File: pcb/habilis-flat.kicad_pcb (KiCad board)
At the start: 2 copper layers, 164 x 172.3 mm, 74 parts, among them SW1 MX, SW10 MX, SW11 MX, SW12 MX, SW13 MX, SW14 MX, SW15 MX, SW16 MX, SW17 MX, SW18 MX, SW19 MX, SW2 MX, SW20 MX, SW21 MX, SW22 MX, SW23 MX, SW24 MX, SW25 MX, SW26 MX, SW27 MX, SW28 MX, SW29 MX, SW3 MX, SW30 MX, SW31 MX, SW32 MX, SW33 MX, SW34 MX, SW35 MX, SW4 MX, SW5 MX, SW6 MX, SW7 MX, SW8 MX, SW9 MX, U1 ProMicro

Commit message: Simplify schematic, update diode footprint reference
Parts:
- renumbered TRRS_L to J1, TRRS_R to J2
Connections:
- net Net-(D1-K) renamed row1
- net Net-(D10-K) renamed row5
- net Net-(D12-K) renamed row2
- net Net-(D13-K) renamed row3
- net Net-(D14-K) renamed row4
- net Net-(U1-B4) renamed col2
- net Net-(U1-B5) renamed col1
- net Net-(U1-C6) renamed col5
- net Net-(U1-D4) renamed col6
- net Net-(U1-D7) renamed col4
- net Net-(U1-E6) renamed col3
- net Net-(U1-F6) renamed col7

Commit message: Update PCB
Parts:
- TRRS1: renamed from J1; value AudioJack4 -> Left TRRS cable
- TRRS2: renamed from J2; value AudioJack4 -> Right TRRS cable

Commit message: Realign thumb cluster keys
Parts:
- moved SW31 19.6 mm to (125.3, 93.6)
- moved SW32 19.6 mm to (139.5, 107.3)
- moved D31 16.1 mm to (125.5, 90.0)
- moved D32 16.1 mm to (136.8, 101.5)
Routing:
- net row1: track 238.2 -> 220.3 mm
- net row2: track 221.3 -> 238.9 mm
- net Net-(D32-A): track 9.79 -> 7.63 mm
- net Net-(D31-A): track 7.63 -> 9.79 mm

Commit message: Cleanup some tracks
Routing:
- net row2: track 238.9 -> 245.7 mm

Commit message: Move copyright to a nicer place
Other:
- board text added: "(yet another"
- board text added: "keyboard)"
- board text added: "© Thibault Polge 2023 https://thb.lt"
- board text removed: "Copyright © 2023 Thibault Polge https://thb.lt/"
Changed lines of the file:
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@@
   (gr_line (start 149.588485 105.669449) (end 133.956727 96.644449)
     (stroke (width 0.2) (type solid)) (layer "Edge.Cuts"))
-  (gr_text "Copyright © 2023 Thibault Polge https://thb.lt/" (at 65.90965 48.470207 90) (layer "B.SilkS")
-    (effects (font (size 1 1) (thickness 0.15)) (justify left bottom mirror))
-  )
   (gr_text "FLAT" (at 54.541406 -12.165028) (layer "B.SilkS")
     (effects (font (size 2 2) (thickness 0.2)) (justify left bottom mirror))
@@
     (effects (font (size 2 2) (thickness 0.2)) (justify left bottom mirror))
   )
+  (gr_text "© Thibault Polge \n2023 https://thb.lt" (at 75.63002 -13.373041) (layer "B.SilkS")
+    (effects (font (size 1 1) (thickness 0.15)) (justify right bottom mirror))
+  )
+  (gr_text "(yet another\n" (at 82.886942 -19.195307) (layer "F.SilkS")
+    (effects (font (size 1 1) (thickness 0.15)) (justify bottom))
+  )
+  (gr_text "HABILIS" (at 81.410346 -20.657928) (layer "F.SilkS" knockout)
+    (effects (font (size 1 1) (thickness 0.15)) (justify left bottom))
+  )
+  (gr_text "keyboard)" (at 80.949201 -18.096012) (layer "F.SilkS")
+    (effects (font (size 1 1) (thickness 0.15)) (justify left bottom))
+  )
   (segment (start 1.27 2.54) (end 1.27 0.633604) (width 0.25) (layer "F.Cu") (net 1))

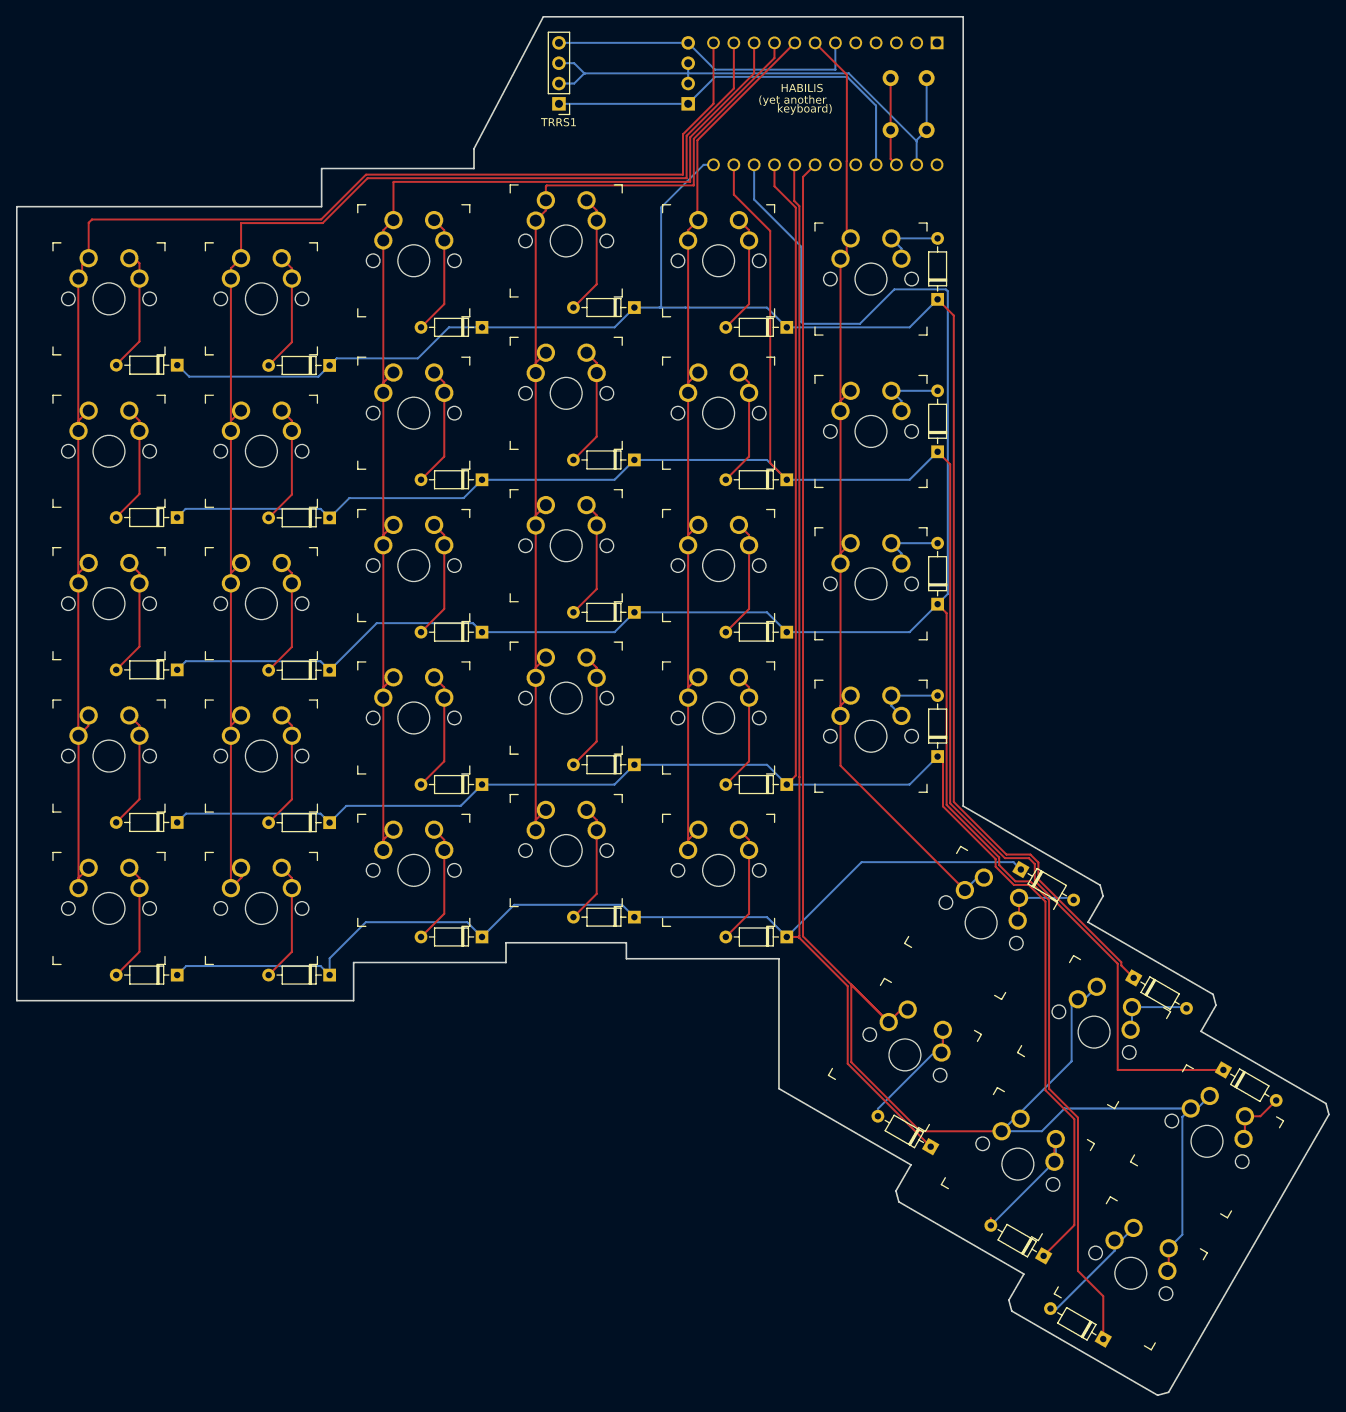
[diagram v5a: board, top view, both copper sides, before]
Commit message: Restore mounting holes
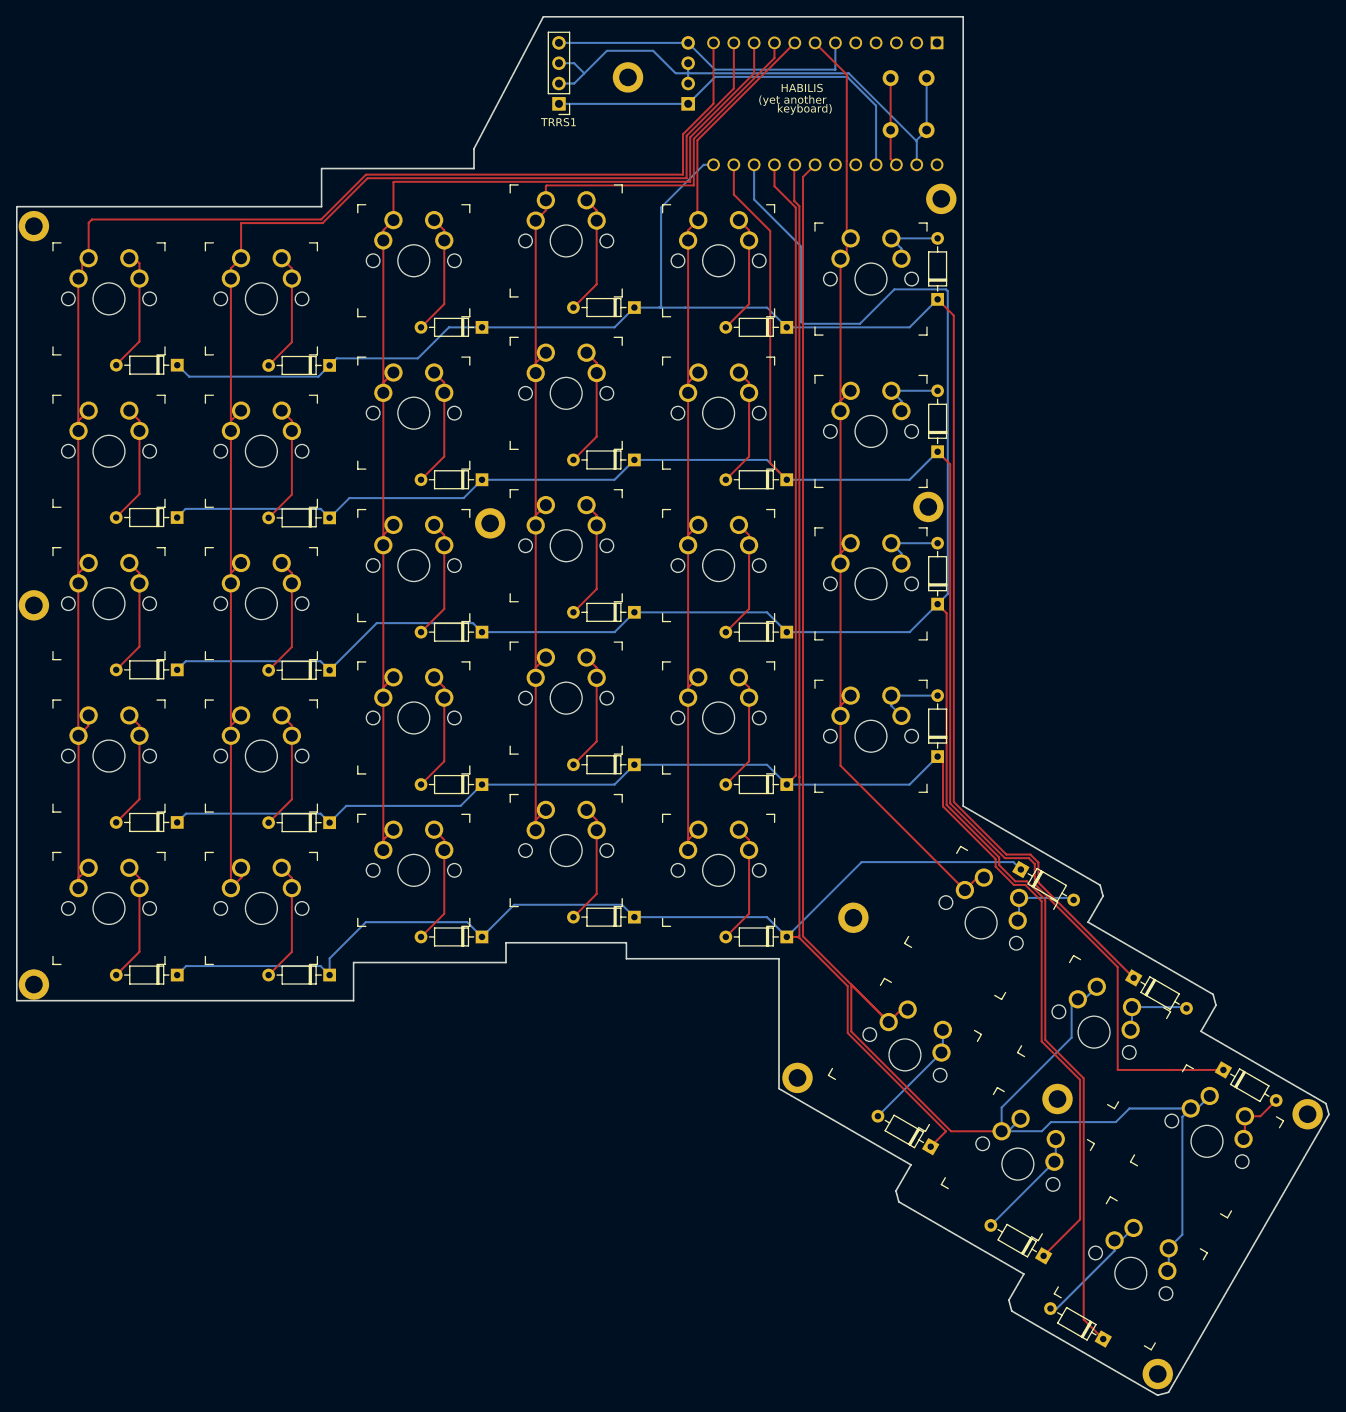
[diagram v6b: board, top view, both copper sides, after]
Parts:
- added REF**: MountingHole_2.2mm_M2_DIN965_Pad_NO_Silkscreem, project-components:MountingHole_2.2mm_M2_DIN965_Pad_NO_Silkscreem, F.Cu at (101.5, -7.41)
- added REF**: MountingHole_2.2mm_M2_DIN965_Pad_NO_Silkscreem, project-components:MountingHole_2.2mm_M2_DIN965_Pad_NO_Silkscreem, F.Cu at (83.5, 102.5)
- added REF**: MountingHole_2.2mm_M2_DIN965_Pad_NO_Silkscreem, project-components:MountingHole_2.2mm_M2_DIN965_Pad_NO_Silkscreem, F.Cu at (62.3, -22.6)
- added REF**: MountingHole_2.2mm_M2_DIN965_Pad_NO_Silkscreem, project-components:MountingHole_2.2mm_M2_DIN965_Pad_NO_Silkscreem, F.Cu at (128.6, 139.5)
- added REF**: MountingHole_2.2mm_M2_DIN965_Pad_NO_Silkscreem, project-components:MountingHole_2.2mm_M2_DIN965_Pad_NO_Silkscreem, F.Cu at (90.5, 82.4)
- added REF**: MountingHole_2.2mm_M2_DIN965_Pad_NO_Silkscreem, project-components:MountingHole_2.2mm_M2_DIN965_Pad_NO_Silkscreem, F.Cu at (99.9, 31.1)
- added REF**: MountingHole_2.2mm_M2_DIN965_Pad_NO_Silkscreem, project-components:MountingHole_2.2mm_M2_DIN965_Pad_NO_Silkscreem, F.Cu at (116.0, 105.1)
- added REF**: MountingHole_2.2mm_M2_DIN965_Pad_NO_Silkscreem, project-components:MountingHole_2.2mm_M2_DIN965_Pad_NO_Silkscreem, F.Cu at (147.3, 107.0)
- added REF**: MountingHole_2.2mm_M2_DIN965_Pad_NO_Silkscreem, project-components:MountingHole_2.2mm_M2_DIN965_Pad_NO_Silkscreem, F.Cu at (-11.9, 43.4)
- added REF**: MountingHole_2.2mm_M2_DIN965_Pad_NO_Silkscreem, project-components:MountingHole_2.2mm_M2_DIN965_Pad_NO_Silkscreem, F.Cu at (-11.9, 90.8)
- added REF**: MountingHole_2.2mm_M2_DIN965_Pad_NO_Silkscreem, project-components:MountingHole_2.2mm_M2_DIN965_Pad_NO_Silkscreem, F.Cu at (45.1, 33.1)
- added REFe: MountingHole_2.2mm_M2_DIN965_Pad_NO_Silkscreem, project-components:MountingHole_2.2mm_M2_DIN965_Pad_NO_Silkscreem, F.Cu at (-11.9, -4.01)
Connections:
- D1 pad 1: row1 -> row0
- D10 pad 1: row5 -> row4
- D11 pad 1: row1 -> row0
- D12 pad 1: row2 -> row1
- D13 pad 1: row3 -> row2
- D14 pad 1: row4 -> row3
- D15 pad 1: row5 -> row4
- D16 pad 1: row1 -> row0
- D17 pad 1: row2 -> row1
- D18 pad 1: row3 -> row2
- D19 pad 1: row4 -> row3
- D2 pad 1: row2 -> row1
- D20 pad 1: row5 -> row4
- D21 pad 1: row1 -> row0
- D22 pad 1: row2 -> row1
- D23 pad 1: row3 -> row2
- D24 pad 1: row4 -> row3
- D25 pad 1: row5 -> row4
- D26 pad 1: row1 -> row0
- D27 pad 1: row2 -> row1
- D28 pad 1: row3 -> row2
- D29 pad 1: row4 -> row3
- D3 pad 1: row3 -> row2
- D30 pad 1: row5 -> row4
- D31 pad 1: row1 -> row0
- D32 pad 1: row2 -> row1
- D33 pad 1: row3 -> row2
- D34 pad 1: row4 -> row3
- D35 pad 1: row5 -> row4
- D4 pad 1: row4 -> row3
- D5 pad 1: row5 -> row4
- D6 pad 1: row1 -> row0
- D7 pad 1: row2 -> row1
- D8 pad 1: row3 -> row2
- D9 pad 1: row4 -> row3
- SW1 pad 2: col1 -> col0
- SW10 pad 2: col2 -> col1
- SW11 pad 2: col3 -> col2
- SW12 pad 2: col3 -> col2
- SW13 pad 2: col3 -> col2
- SW14 pad 2: col3 -> col2
- SW15 pad 2: col3 -> col2
- SW16 pad 2: col4 -> col3
- SW17 pad 2: col4 -> col3
- SW18 pad 2: col4 -> col3
- SW19 pad 2: col4 -> col3
- SW2 pad 2: col1 -> col0
- SW20 pad 2: col4 -> col3
- SW21 pad 2: col5 -> col4
- SW22 pad 2: col5 -> col4
- SW23 pad 2: col5 -> col4
- SW24 pad 2: col5 -> col4
- SW25 pad 2: col5 -> col4
- SW26 pad 2: col6 -> col5
- SW27 pad 2: col6 -> col5
- SW28 pad 2: col6 -> col5
- SW29 pad 2: col6 -> col5
- SW3 pad 2: col1 -> col0
- SW30 pad 2: col6 -> col5
- SW31 pad 2: col7 -> col6
- SW32 pad 2: col7 -> col6
- SW33 pad 1: col7 -> col6
- SW34 pad 2: col7 -> col6
- SW35 pad 2: col7 -> col6
- SW4 pad 2: col1 -> col0
- SW5 pad 2: col1 -> col0
- SW6 pad 2: col2 -> col1
- SW7 pad 2: col2 -> col1
- SW8 pad 2: col2 -> col1
- SW9 pad 2: col2 -> col1
- U1 pad 10: col3 -> col2
- U1 pad 11: col2 -> col1
- U1 pad 12: col1 -> col0
- U1 pad 13: row1 -> row0
- U1 pad 14: row2 -> row1
- U1 pad 15: row3 -> row2
- U1 pad 16: row4 -> row3
- U1 pad 17: row5 -> row4
- U1 pad 18: col7 -> col6
- U1 pad 7: col6 -> col5
- U1 pad 8: col5 -> col4
- U1 pad 9: col4 -> col3
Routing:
- net row5: track 250.2 -> 0.00 mm
- net col7: track 226.7 -> 0.00 mm
- net row0: track 0.00 -> 220.3 mm
- net col0: track 0.00 -> 191.3 mm
- net col6: track 126.9 -> 227.7 mm
- net row2: track 245.7 -> 285.7 mm
- net row3: track 285.9 -> 253.0 mm
- net row1: track 220.3 -> 245.7 mm
- net col3: track 154.2 -> 133.8 mm
- net col2: track 173.4 -> 154.2 mm
- net col1: track 191.3 -> 173.4 mm
- net col4: track 133.8 -> 118.8 mm
- net col5: track 118.8 -> 127.7 mm
- net Net-(D34-A): track 18.0 -> 14.4 mm
- net Net-(D35-A): track 16.7 -> 13.3 mm
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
